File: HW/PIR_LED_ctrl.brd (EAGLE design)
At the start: 100 x 80 mm, 6 parts, among them J1 POWER_JACKPTH

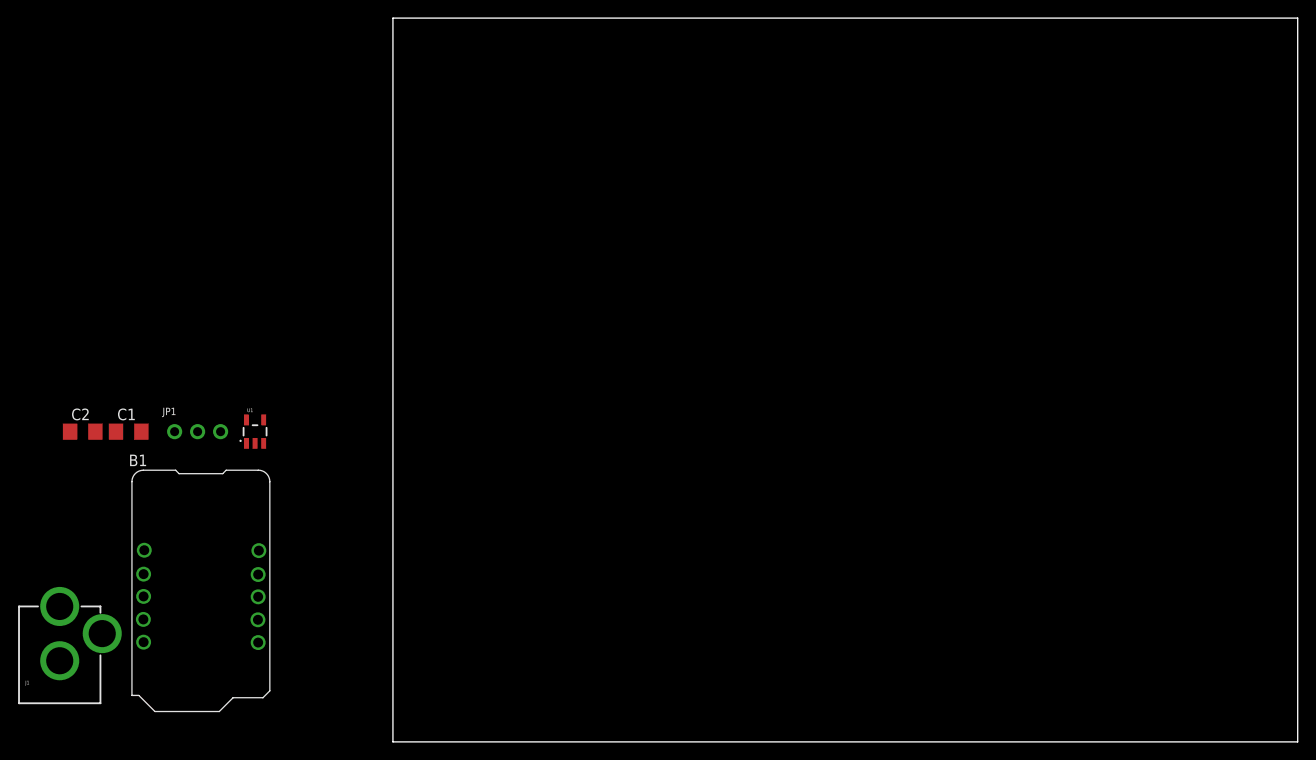
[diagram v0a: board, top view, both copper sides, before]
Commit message: added holes and released everything
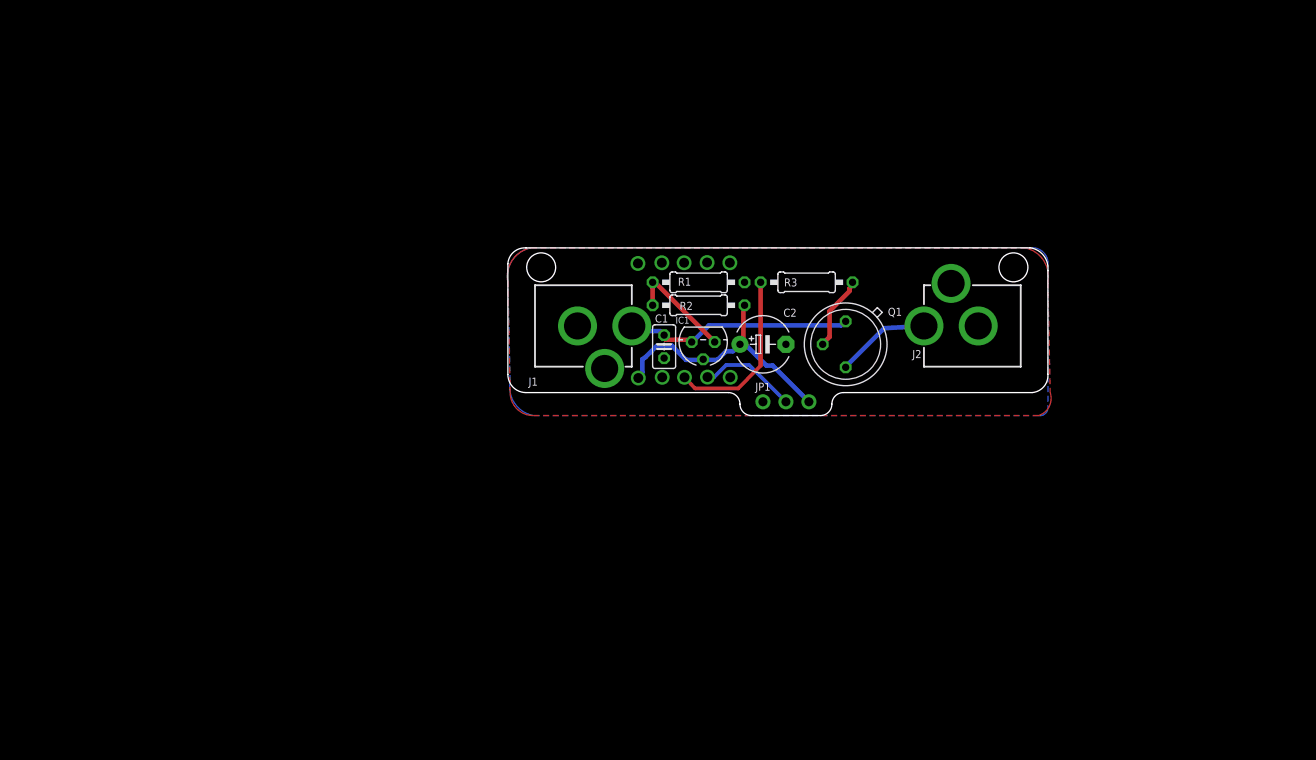
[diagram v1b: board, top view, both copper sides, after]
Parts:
- removed U1: (no value), pero_library:SOT23-5
- added IC1: LM317LZ, linear:TO92
- added J2: LED Strip, SparkFun-Connectors:POWER_JACK_PTH
- added Q1: 2N2905, transistor:TO39
- added R1: 10k, rcl:0207/10
- added R2: 30k, rcl:0207/10
- added R3: 1k, rcl:0207/10
- added U$1: (no value), frames:A5L-LOC
- C1: value (none) -> 0.1uF; device rcl:C1206 -> rcl:C025-025X050
- C2: value (none) -> 1uF; device rcl:C1206 -> rcl:E5-6
- J1: value POWER_JACKPTH -> POWER_IN
- JP1: value (none) -> PIR
- moved C2 75.8 mm to (40.9, 43.9)
- moved J1 66.7 mm to (12.7, 46.0), turned to 270 degrees
- moved JP1 65.1 mm to (43.4, 37.6), turned to 180 degrees
- moved B1 61.4 mm to (31.8, 47.0), flipped to the bottom, turned to 270 degrees
- moved C1 59.9 mm to (30.0, 43.7), turned to 90 degrees
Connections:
- new net N$1: IC1.1, R1.1, R2.2
- new net N$3: B1.8, R3.1
- new net N$4: Q1.2, R3.2
- net 12V: now also IC1.3, Q1.1; no longer U1.1, U1.3
- net 5V: now also C2.+, IC1.2, R1.2
- net GND: now also C2.-, J2.GND, J2.GNDBREAK, R2.1; no longer C2.1, U1.2
- net N$2: now also J2.PWR, Q1.3; no longer C2.2, U1.5
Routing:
- net 5V: track 0.00 -> 30.2 mm
- net 12V: track 0.00 -> 25.8 mm
- net N$3: track 0.00 -> 19.2 mm
- net N$1: track 0.00 -> 13.5 mm
- net PIR: track 0.00 -> 10.9 mm
- net N$2: track 0.00 -> 10.5 mm
- net N$4: track 0.00 -> 8.21 mm
- added copper zone on layer 1, net GND
- added copper zone on layer 16, net GND
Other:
- board size 100 x 80 mm -> 59.7 x 18.5 mm
- board text added: "Controller board for the motion controlled LED strip."
- board text added: "Motion controlled LED controller"
- board text added: "Pero 2017"
- board text added: "www.helentronica.com"
